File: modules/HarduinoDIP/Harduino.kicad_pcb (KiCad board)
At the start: 2 copper layers, 40.6 x 40.6 mm, 30 parts, among them J1 2, J10 11, J11 12, J12 13, J13 A0, J14 A1, J15 A2, J16 A3, J17 A4, J18 A5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

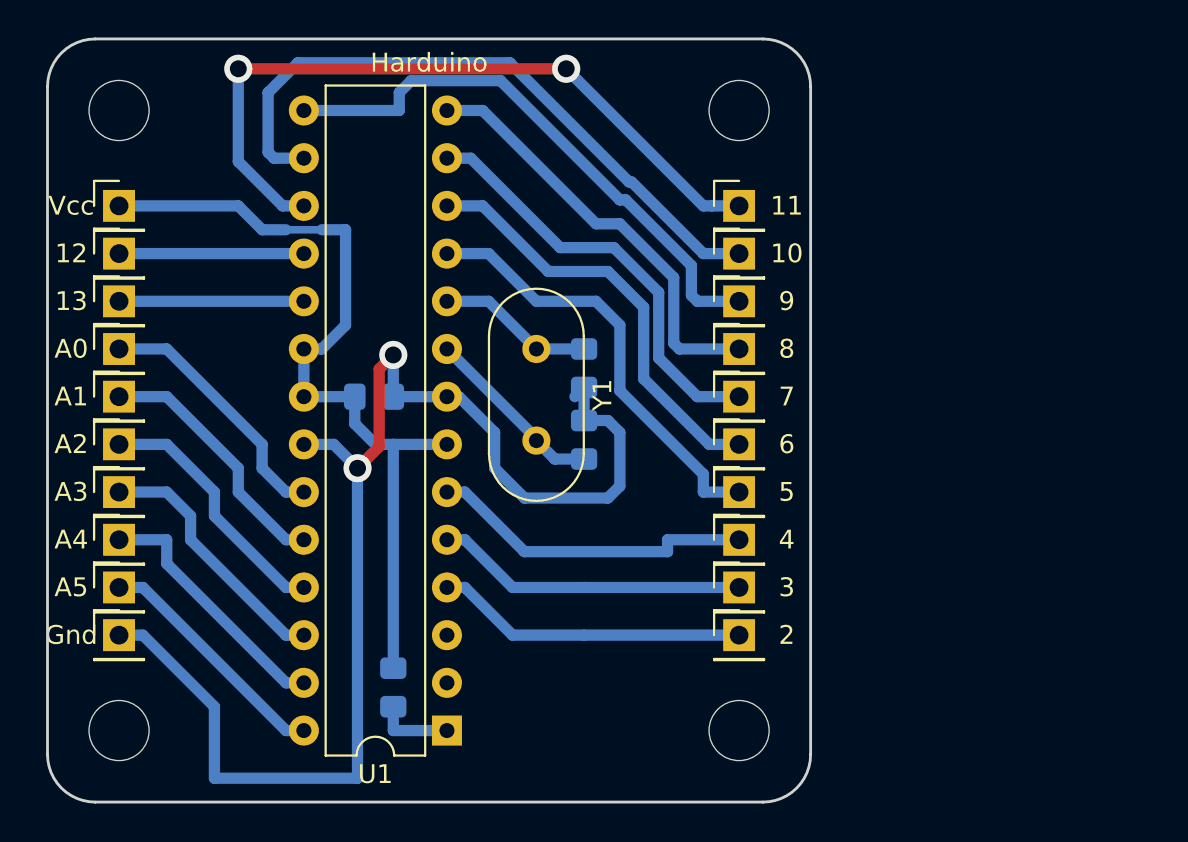
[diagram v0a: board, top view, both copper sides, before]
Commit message: HarduinoDIP in work
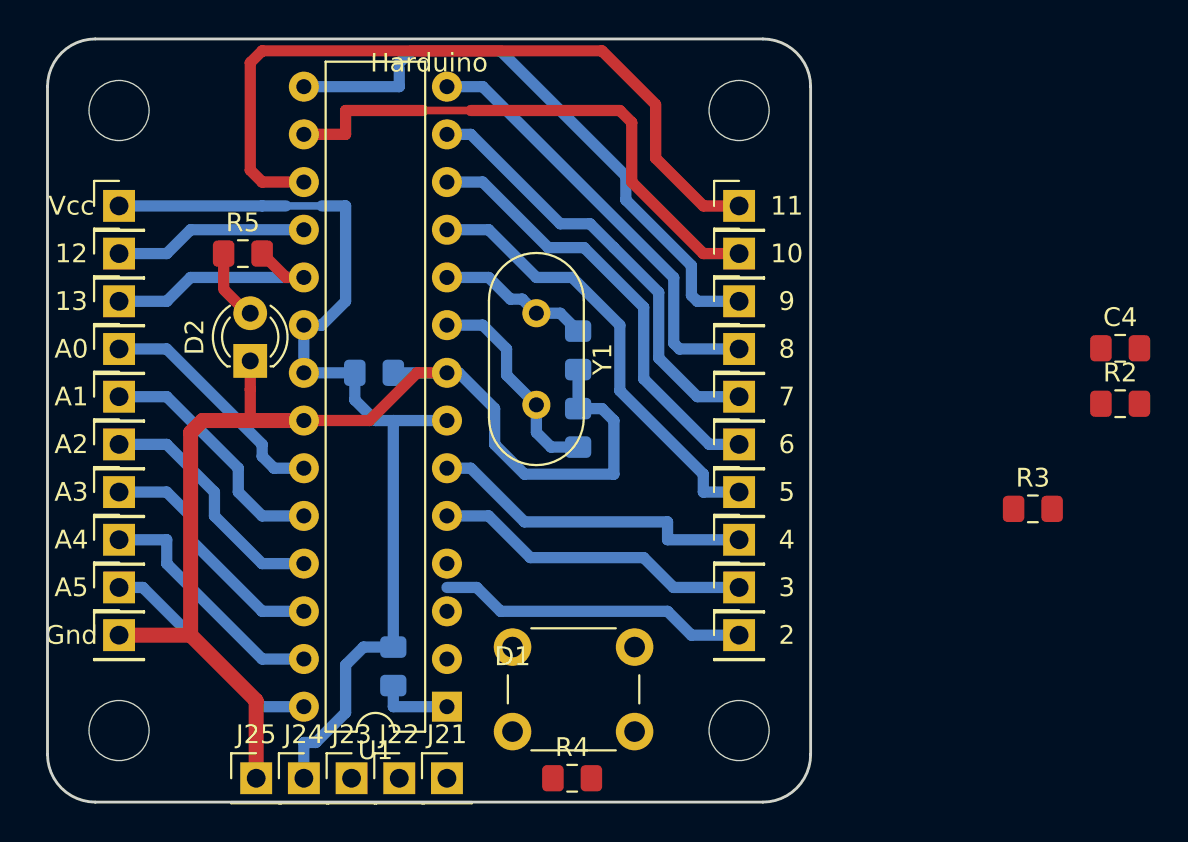
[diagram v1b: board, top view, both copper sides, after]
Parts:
- added C4: 0.1uF, Capacitor_SMD:C_0805_2012Metric_Pad1.15x1.40mm_HandSolder, F.Cu at (146.0, 67.3)
- added D1: 6x6-tact-btn, CommonLibrary:6x6-tact-btn, F.Cu at (113.7, 83.2)
- added D2: LED, LED_THT:LED_D3.0mm, F.Cu at (99.7, 67.9)
- added J21: ~RESET, Connector_PinHeader_2.54mm:PinHeader_1x01_P2.54mm_Vertical, F.Cu at (110.2, 90.2)
- added J22: RX, Connector_PinHeader_2.54mm:PinHeader_1x01_P2.54mm_Vertical, F.Cu at (107.6, 90.2)
- added J23: TX, Connector_PinHeader_2.54mm:PinHeader_1x01_P2.54mm_Vertical, F.Cu at (105.1, 90.2)
- added J24: Vcc, Connector_PinHeader_2.54mm:PinHeader_1x01_P2.54mm_Vertical, F.Cu at (102.6, 90.2)
- added J25: Gnd, Connector_PinHeader_2.54mm:PinHeader_1x01_P2.54mm_Vertical, F.Cu at (100.0, 90.2)
- added R2: 1k, Resistor_SMD:R_0805_2012Metric_Pad1.15x1.40mm_HandSolder, F.Cu at (146.0, 70.2)
- added R3: 1k, Resistor_SMD:R_0805_2012Metric_Pad1.15x1.40mm_HandSolder, F.Cu at (141.4, 75.8)
- added R4: 1k, Resistor_SMD:R_0805_2012Metric_Pad1.15x1.40mm_HandSolder, F.Cu at (116.8, 90.2)
- added R5: 1k, Resistor_SMD:R_0805_2012Metric_Pad1.15x1.40mm_HandSolder, F.Cu at (99.3, 62.2)
- moved Y1 1.91 mm to (114.9, 65.4)
- moved C1 1.27 mm to (106.3, 68.6)
- moved U1 1.27 mm to (110.2, 86.4)
- moved R1 1.12 mm to (107.3, 84.2)
- moved C2 1.00 mm to (117.2, 67.4)
- moved C3 0.71 mm to (117.2, 71.5)
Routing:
- net VCC: track 44.4 -> 54.1 mm
- net GND: track 70.2 -> 64.0 mm, vias 2 -> 0
- net Net-(J9-Pad1): track 35.2 -> 29.5 mm
- net Net-(D2-Pad2): track 0.00 -> 3.76 mm
- net Net-(J12-Pad1): track 9.84 -> 13.1 mm
- net Net-(C3-Pad1): track 9.80 -> 11.3 mm
- net Net-(J8-Pad1): track 30.2 -> 31.6 mm
- net Net-(J10-Pad1): track 39.1 -> 40.2 mm, vias 2 -> 0
- net Net-(J13-Pad1): track 13.7 -> 12.8 mm
- net Net-(C2-Pad1): track 8.80 -> 8.17 mm
- net Net-(J15-Pad1): track 13.7 -> 13.2 mm
- net Net-(J17-Pad1): track 13.7 -> 13.2 mm
- net Net-(J7-Pad1): track 22.9 -> 23.4 mm
- net Net-(J4-Pad1): track 23.4 -> 23.9 mm
- net Net-(J16-Pad1): track 13.7 -> 13.2 mm
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
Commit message: Harduino in work
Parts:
- C4, R4: moved to B.Cu
- moved R2 41.3 mm to (107.1, 83.8)
- moved R3 36.2 mm to (105.4, 80.0)
- moved C4 35.0 mm to (116.8, 86.6), turned to 90 degrees
- moved R4 1.20 mm to (118.0, 90.2)
- moved D1 0.40 mm to (113.5, 82.8)
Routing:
- net Net-(C4-Pad2): track 4.13 -> 13.7 mm
- net Net-(C4-Pad1): track 0.00 -> 9.45 mm
- net GND: track 64.0 -> 67.3 mm
- net Net-(J3-Pad1): track 17.7 -> 17.1 mm
- net Net-(J1-Pad1): track 16.6 -> 17.1 mm

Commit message: Trace it! Harduino ready.
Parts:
- moved R3 2.47 mm to (105.4, 82.5), turned to 90 degrees
- moved R2 0.46 mm to (107.3, 84.2), turned to 90 degrees
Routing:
- net GND: track 67.3 -> 95.9 mm
- net Net-(J23-Pad1): track 0.00 -> 6.80 mm
- net Net-(C4-Pad2): track 13.7 -> 20.2 mm
- net Net-(J22-Pad1): track 0.00 -> 5.07 mm
- net Net-(R3-Pad2): track 0.00 -> 4.83 mm
- net Net-(R2-Pad2): track 0.00 -> 3.12 mm
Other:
- board text added: "DTR"
- board text added: "RX"
- board text added: "TX"

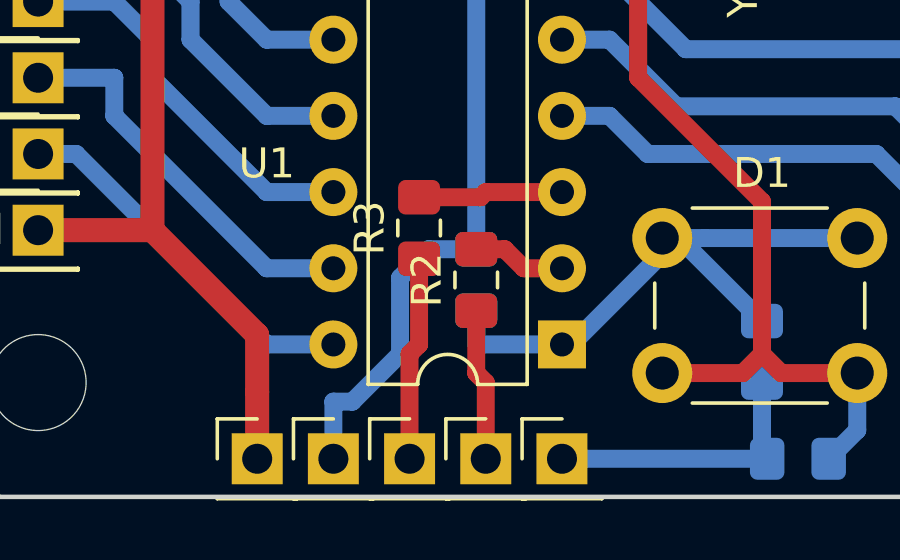
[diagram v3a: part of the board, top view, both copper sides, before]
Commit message: Fix RX/TX pins order
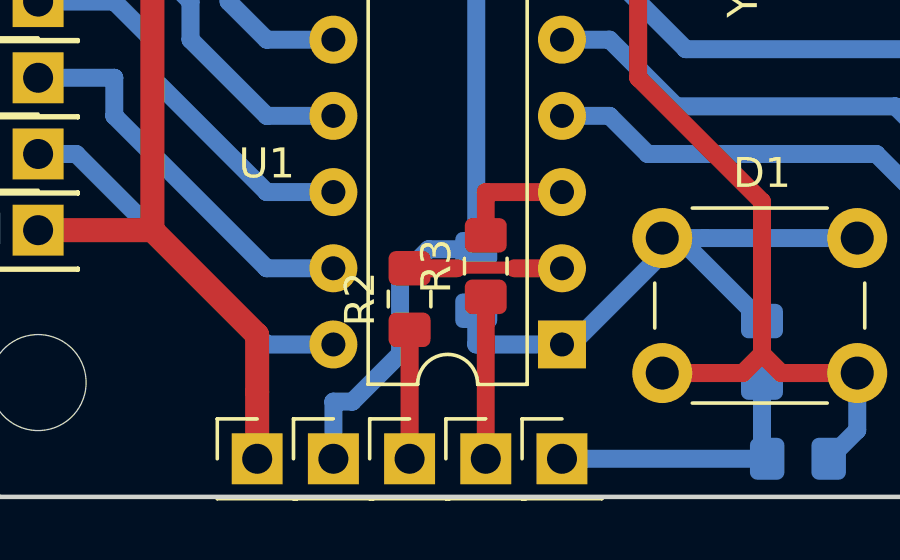
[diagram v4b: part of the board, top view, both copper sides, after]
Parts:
- moved R3 2.56 mm to (107.6, 83.7)
- moved J22 2.54 mm to (105.1, 90.2)
- moved J23 2.54 mm to (107.6, 90.2)
- moved R2 2.31 mm to (105.1, 84.8)
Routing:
- net Net-(R2-Pad2): track 3.12 -> 5.10 mm
- net Net-(J23-Pad1): track 6.80 -> 5.40 mm
- net Net-(R3-Pad2): track 4.83 -> 3.98 mm
- net Net-(J22-Pad1): track 5.07 -> 4.30 mm
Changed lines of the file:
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@@
     (thickness 1.6)
     (drawings 34)
-    (tracks 199)
+    (tracks 197)
     (zones 0)
     (modules 42)
@@
   )
   (module Connector_PinHeader_2.54mm:PinHeader_1x01_P2.54mm_Vertical (layer F.Cu)
+    (at 105.0925 90.17)
+    (descr "Through hole straight pin header, 1x01, 2.54mm pitch, single row")
+    (tags "Through hole pin header THT 1x01 2.54mm single row")
+    (fp_text reference J22 (at 0 -2.33) (layer F.SilkS) hide
+      (effects (font (size 1 1) (thickness 0.15)))
+    )
+    (fp_text value RX (at 0 2.33) (layer F.Fab)
+      (effects (font (size 1 1) (thickness 0.15)))
+    )
+    (fp_line (start -0.635 -1.27) (end 1.27 -1.27) (layer F.Fab) (width 0.1))
+    (fp_line (start 1.27 -1.27) (end 1.27 1.27) (layer F.Fab) (width 0.1))
+    (fp_line (start 1.27 1.27) (end -1.27 1.27) (layer F.Fab) (width 0.1))
+    (fp_line (start -1.27 1.27) (end -1.27 -0.635) (layer F.Fab) (width 0.1))
+    (fp_line (start -1.27 -0.635) (end -0.635 -1.27) (layer F.Fab) (width 0.1))
+    (fp_line (start -1.33 1.33) (end 1.33 1.33) (layer F.SilkS) (width 0.12))
+    (fp_line (start -1.33 1.27) (end -1.33 1.33) (layer F.SilkS) (width 0.12))
+    (fp_line (start 1.33 1.27) (end 1.33 1.33) (layer F.SilkS) (width 0.12))
+    (fp_line (start -1.33 1.27) (end 1.33 1.27) (layer F.SilkS) (width 0.12))
+    (fp_line (start -1.33 0) (end -1.33 -1.33) (layer F.SilkS) (width 0.12))
+    (fp_line (start -1.33 -1.33) (end 0 -1.33) (layer F.SilkS) (width 0.12))
+    (fp_line (start -1.8 -1.8) (end -1.8 1.8) (layer F.CrtYd) (width 0.05))
+    (fp_line (start -1.8 1.8) (end 1.8 1.8) (layer F.CrtYd) (width 0.05))
+    (fp_line (start 1.8 1.8) (end 1.8 -1.8) (layer F.CrtYd) (width 0.05))
+    (fp_line (start 1.8 -1.8) (end -1.8 -1.8) (layer F.CrtYd) (width 0.05))
+    (fp_text user %R (at 0 0 90) (layer F.Fab)
+      (effects (font (size 1 1) (thickness 0.15)))
+    )
+    (pad 1 thru_hole rect (at 0 0) (size 1.7 1.7) (drill 1) (layers *.Cu *.Mask)
+      (net 26 "Net-(J22-Pad1)"))
+    (model ${KISYS3DMOD}/Connector_PinHeader_2.54mm.3dshapes/PinHeader_1x01_P2.54mm_Vertical.wrl
+      (at (xyz 0 0 0))
+      (scale (xyz 1 1 1))
+      (rotate (xyz 0 0 0))
+    )
+  )
+  (module Connector_PinHeader_2.54mm:PinHeader_1x01_P2.54mm_Vertical (layer F.Cu)
     (at 107.6325 90.17)
     (descr "Through hole straight pin header, 1x01, 2.54mm pitch, single row")
     (tags "Through hole pin header THT 1x01 2.54mm single row")
-    (fp_text reference J22 (at 0 -2.33) (layer F.SilkS) hide
-      (effects (font (size 1 1) (thickness 0.15)))
-    )
-    (fp_text value RX (at 0 2.33) (layer F.Fab)
-      (effects (font (size 1 1) (thickness 0.15)))
-    )
-    (fp_line (start -0.635 -1.27) (end 1.27 -1.27) (layer F.Fab) (width 0.1))
-    (fp_line (start 1.27 -1.27) (end 1.27 1.27) (layer F.Fab) (width 0.1))
-    (fp_line (start 1.27 1.27) (end -1.27 1.27) (layer F.Fab) (width 0.1))
-    (fp_line (start -1.27 1.27) (end -1.27 -0.635) (layer F.Fab) (width 0.1))
-    (fp_line (start -1.27 -0.635) (end -0.635 -1.27) (layer F.Fab) (width 0.1))
-    (fp_line (start -1.33 1.33) (end 1.33 1.33) (layer F.SilkS) (width 0.12))
-    (fp_line (start -1.33 1.27) (end -1.33 1.33) (layer F.SilkS) (width 0.12))
-    (fp_line (start 1.33 1.27) (end 1.33 1.33) (layer F.SilkS) (width 0.12))
-    (fp_line (start -1.33 1.27) (end 1.33 1.27) (layer F.SilkS) (width 0.12))
-    (fp_line (start -1.33 0) (end -1.33 -1.33) (layer F.SilkS) (width 0.12))
-    (fp_line (start -1.33 -1.33) (end 0 -1.33) (layer F.SilkS) (width 0.12))
-    (fp_line (start -1.8 -1.8) (end -1.8 1.8) (layer F.CrtYd) (width 0.05))
-    (fp_line (start -1.8 1.8) (end 1.8 1.8) (layer F.CrtYd) (width 0.05))
-    (fp_line (start 1.8 1.8) (end 1.8 -1.8) (layer F.CrtYd) (width 0.05))
-    (fp_line (start 1.8 -1.8) (end -1.8 -1.8) (layer F.CrtYd) (width 0.05))
-    (fp_text user %R (at 0 0 90) (layer F.Fab)
-      (effects (font (size 1 1) (thickness 0.15)))
-    )
-    (pad 1 thru_hole rect (at 0 0) (size 1.7 1.7) (drill 1) (layers *.Cu *.Mask)
-      (net 26 "Net-(J22-Pad1)"))
-    (model ${KISYS3DMOD}/Connector_PinHeader_2.54mm.3dshapes/PinHeader_1x01_P2.54mm_Vertical.wrl
-      (at (xyz 0 0 0))
-      (scale (xyz 1 1 1))
-      (rotate (xyz 0 0 0))
-    )
-  )
-  (module Connector_PinHeader_2.54mm:PinHeader_1x01_P2.54mm_Vertical (layer F.Cu)
-    (at 105.0925 90.17)
-    (descr "Through hole straight pin header, 1x01, 2.54mm pitch, single row")
-    (tags "Through hole pin header THT 1x01 2.54mm single row")
     (fp_text reference J23 (at 0 -2.33) (layer F.SilkS) hide
       (effects (font (size 1 1) (thickness 0.15)))
@@
   )
   (module Resistor_SMD:R_0805_2012Metric_Pad1.15x1.40mm_HandSolder (layer F.Cu)
-    (at 107.315 84.21 90)
+    (at 105.0925 84.845 90)
     (descr "Resistor SMD 0805 (2012 Metric), square (rectangular) end terminal, IPC_7351 nominal with elongated pad for handsoldering. (Body size source: https://docs.google.com/spreadsheets/d/1BsfQQcO9C6DZCsRaXUlFlo91Tg2WpOkGARC1WS5S8t0/edit?usp=sharing), generated with kicad-footprint-generator")
     (tags "resistor handsolder")
@@
   )
   (module Resistor_SMD:R_0805_2012Metric_Pad1.15x1.40mm_HandSolder (layer F.Cu)
-    (at 105.41 82.4775 90)
+    (at 107.6325 83.7475 90)
     (descr "Resistor SMD 0805 (2012 Metric), square (rectangular) end terminal, IPC_7351 nominal with elongated pad for handsoldering. (Body size source: https://docs.google.com/spreadsheets/d/1BsfQQcO9C6DZCsRaXUlFlo91Tg2WpOkGARC1WS5S8t0/edit?usp=sharing), generated with kicad-footprint-generator")
     (tags "resistor handsolder")
@@
     (effects (font (size 1 1) (thickness 0.15)) (justify mirror))
   )
-  (gr_text RX (at 107.6325 88.5825) (layer B.SilkS)
+  (gr_text RX (at 105.0925 88.5825) (layer B.SilkS)
     (effects (font (size 1 1) (thickness 0.15)) (justify mirror))
   )
-  (gr_text TX (at 105.0925 88.5825) (layer B.SilkS)
+  (gr_text TX (at 107.6325 88.5825) (layer B.SilkS)
     (effects (font (size 1 1) (thickness 0.15)) (justify mirror))
   )
@@
   (segment (start 98.28 64.135) (end 99.695 65.55) (width 0.6) (layer F.Cu) (net 25))
   (segment (start 98.28 62.23) (end 98.28 63.99) (width 0.6) (layer F.Cu) (net 25))
-  (segment (start 107.315 85.235) (end 107.315 87.3125) (width 0.6) (layer F.Cu) (net 26))
-  (segment (start 107.6325 87.63) (end 107.6325 90.17) (width 0.6) (layer F.Cu) (net 26))
-  (segment (start 107.315 87.3125) (end 107.6325 87.63) (width 0.6) (layer F.Cu) (net 26))
-  (segment (start 105.41 83.5025) (end 105.41 86.36) (width 0.6) (layer F.Cu) (net 27))
-  (segment (start 105.0925 86.6775) (end 105.0925 90.17) (width 0.6) (layer F.Cu) (net 27))
-  (segment (start 105.41 86.36) (end 105.0925 86.6775) (width 0.6) (layer F.Cu) (net 27))
-  (segment (start 107.315 83.185) (end 108.2675 83.185) (width 0.6) (layer F.Cu) (net 28))
-  (segment (start 108.2675 83.185) (end 108.9025 83.82) (width 0.6) (layer F.Cu) (net 28))
-  (segment (start 108.9025 83.82) (end 110.1725 83.82) (width 0.6) (layer F.Cu) (net 28))
-  (segment (start 105.41 81.4525) (end 107.46 81.4525) (width 0.6) (layer F.Cu) (net 29))
+  (segment (start 105.0925 85.87) (end 105.0925 90.17) (width 0.6) (layer F.Cu) (net 26))
+  (segment (start 107.6325 84.7725) (end 107.6325 90.17) (width 0.6) (layer F.Cu) (net 27))
+  (segment (start 105.0925 83.82) (end 106.68 83.82) (width 0.6) (layer F.Cu) (net 28))
+  (segment (start 110.1725 83.82) (end 108.585 83.82) (width 0.6) (layer F.Cu) (net 28))
+  (segment (start 108.56249 83.79749) (end 108.585 83.82) (width 0.4) (layer F.Cu) (net 28))
+  (segment (start 106.913254 83.79749) (end 108.56249 83.79749) (width 0.4) (layer F.Cu) (net 28))
+  (segment (start 106.890744 83.82) (end 106.913254 83.79749) (width 0.4) (layer F.Cu) (net 28))
+  (segment (start 106.68 83.82) (end 106.890744 83.82) (width 0.4) (layer F.Cu) (net 28))
+  (segment (start 107.6325 82.7225) (end 107.6325 81.28) (width 0.6) (layer F.Cu) (net 29))
   (segment (start 107.6325 81.28) (end 110.1725 81.28) (width 0.6) (layer F.Cu) (net 29))
-  (segment (start 107.46 81.4525) (end 107.6325 81.28) (width 0.6) (layer F.Cu) (net 29))
 )

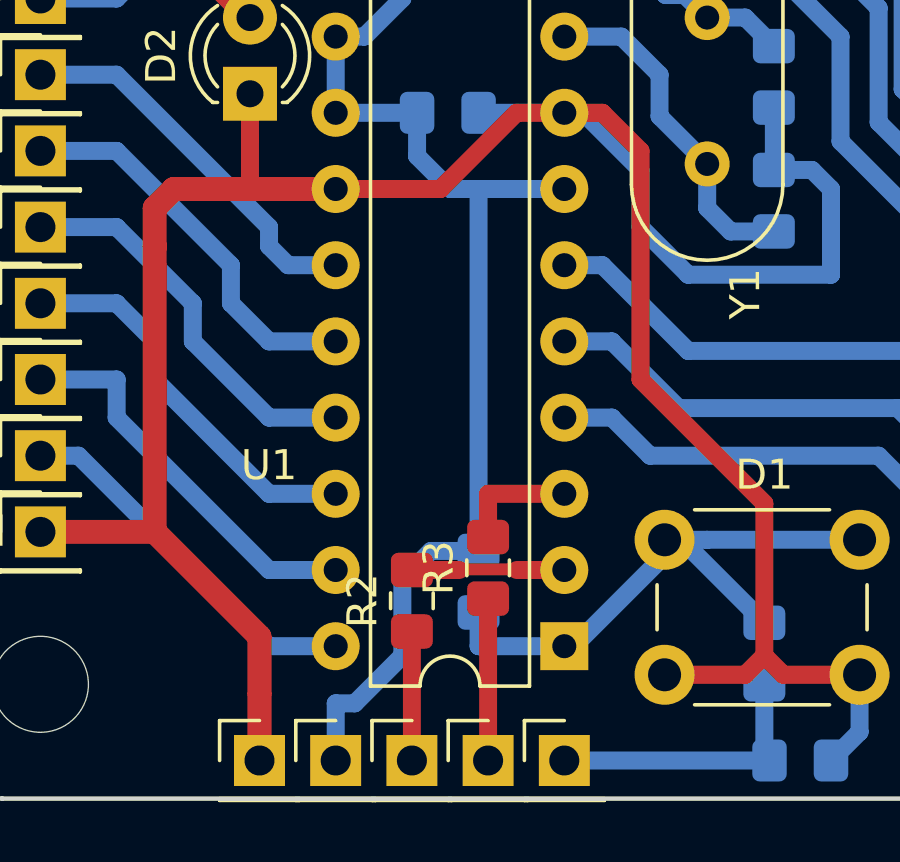
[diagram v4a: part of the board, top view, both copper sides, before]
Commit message: Move R/C to another side
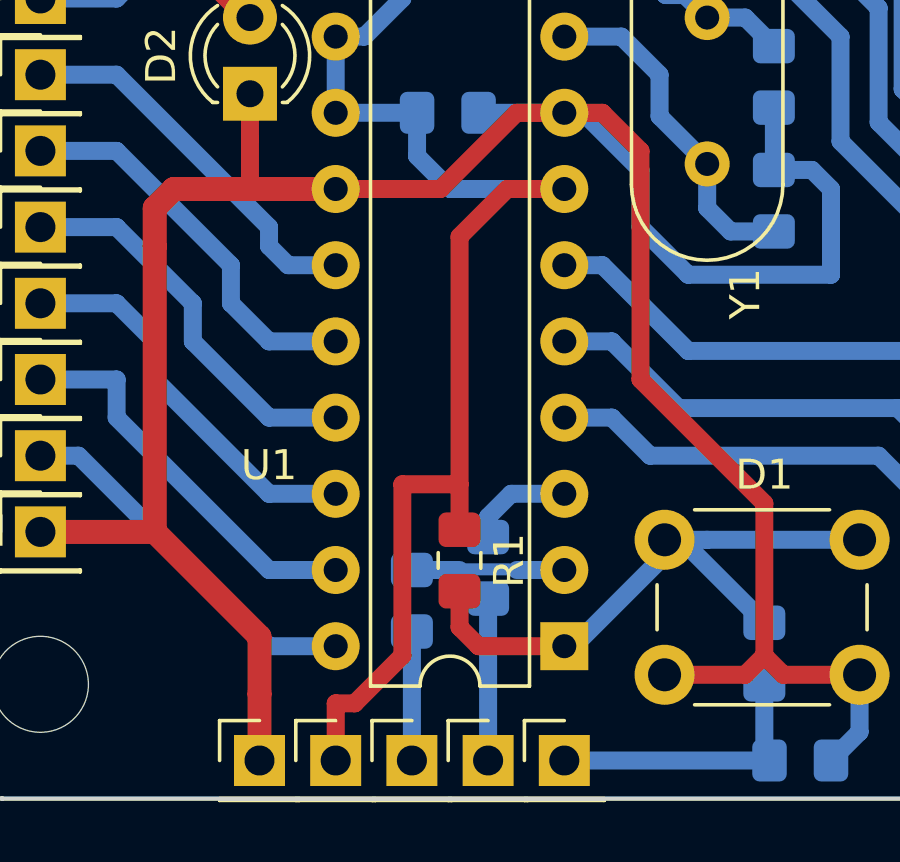
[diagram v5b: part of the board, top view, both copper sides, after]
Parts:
- R1: moved to F.Cu
- R2, R3: moved to B.Cu
- moved R1 0.95 mm to (106.7, 83.5)
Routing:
- net VCC: track 54.1 -> 58.3 mm
- net Net-(C4-Pad2): track 20.2 -> 21.0 mm
